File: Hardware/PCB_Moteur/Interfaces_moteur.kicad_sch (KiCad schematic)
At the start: 47 parts, among them J3 Conn_01x02, J6 Conn_01x06_Pin, U12 MCP1802T-5002I/OT, U2 ISOW1044, U4 LSF0204PWR

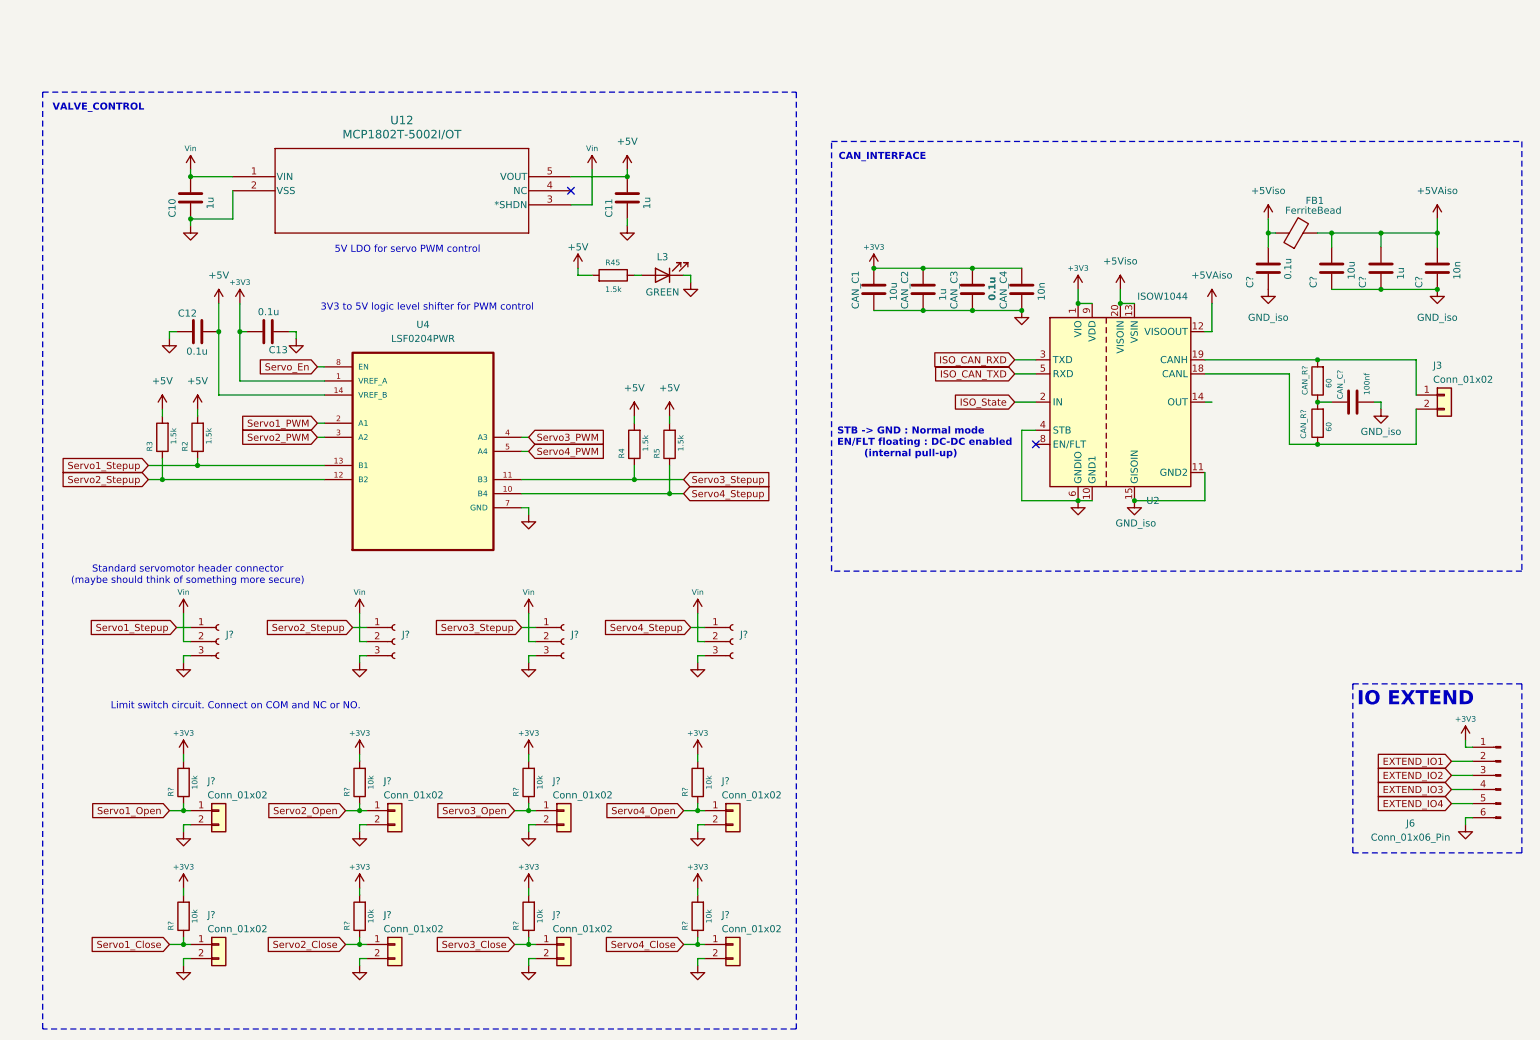
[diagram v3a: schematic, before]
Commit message: fix: LDO 5V SHDN + REFs (missing) + change EN valves controller connection + fix intrumental ampliop + add pull-down to sleep pins
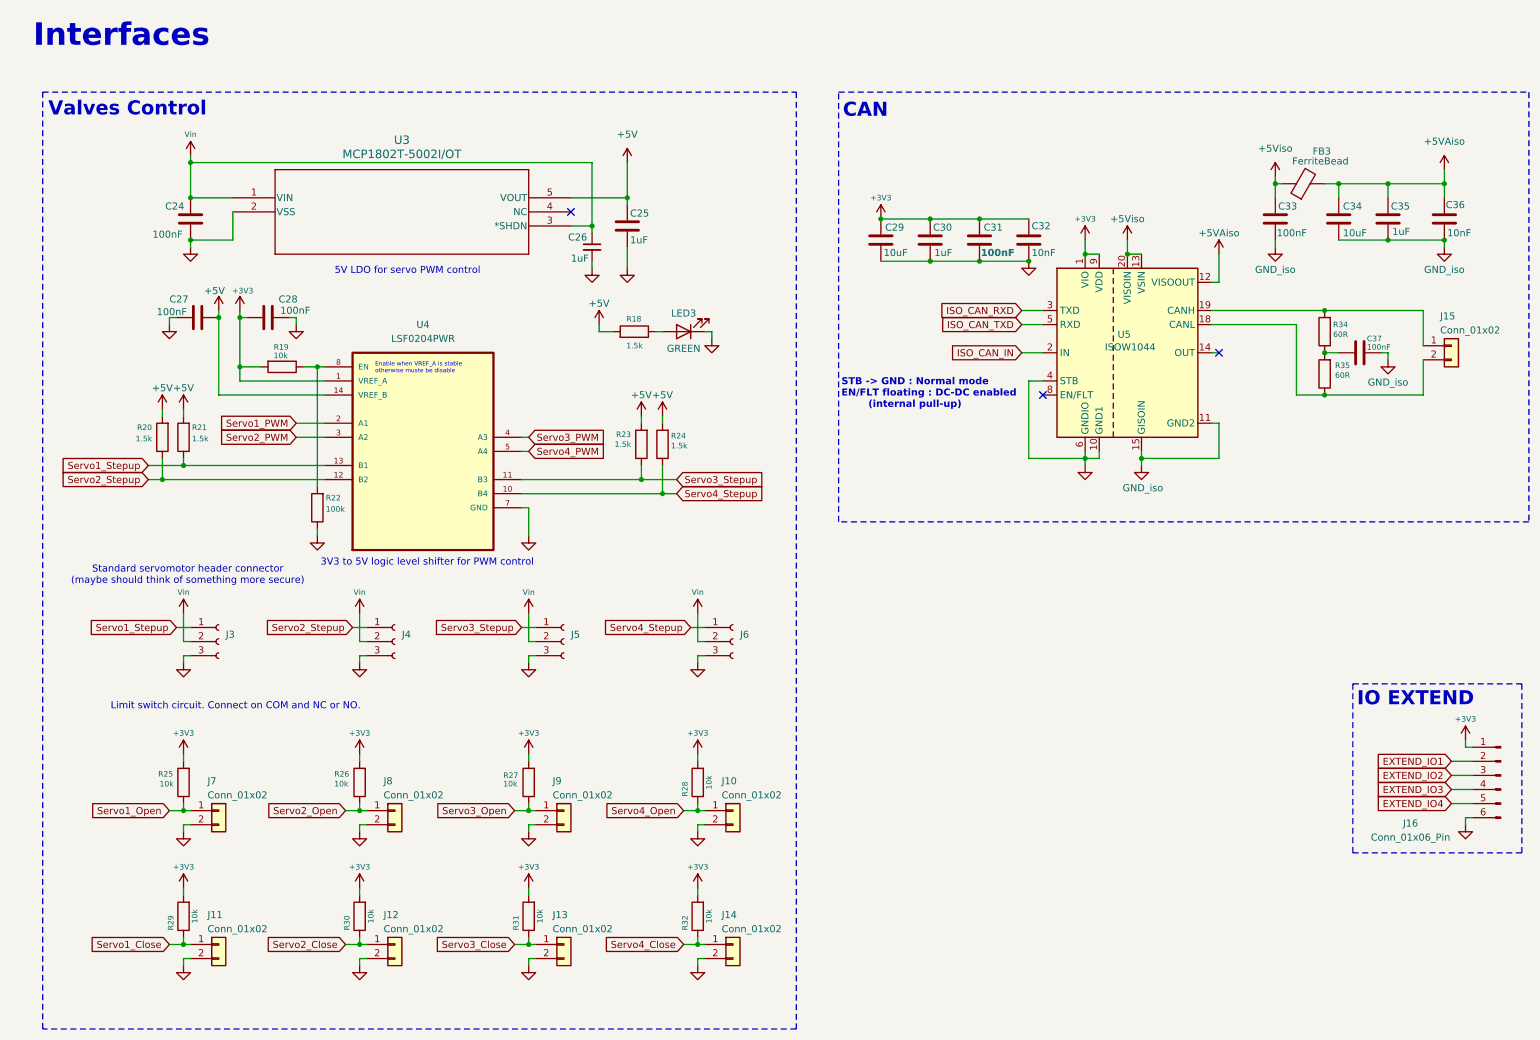
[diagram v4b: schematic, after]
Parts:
- added C26: 1uF, Capacitor_SMD:C_0603_1608Metric, symbol Device:C_Small
- added R19: 10k, Resistor_SMD:R_0805_2012Metric, symbol Device:R
- added R22: 100k, Resistor_SMD:R_0805_2012Metric, symbol Device:R
- C24: renamed from C10; value 1u -> 100nF
- C25: renamed from C11; value 1u -> 1uF
- C27: renamed from C12; value 0.1u -> 100nF
- C28: renamed from C13; value 0.1u -> 100nF
- C29: renamed from CAN_C1; value 10u -> 10uF
- C30: renamed from CAN_C2; value 1u -> 1uF
- C31: renamed from CAN_C3; value 0.1u -> 100nF
- C32: renamed from CAN_C4; value 10n -> 10nF
- C33: renamed from C?; value 0.1u -> 100nF
- C34: renamed from C?; value 10u -> 10uF
- C35: renamed from C?; value 1u -> 1uF
- C36: renamed from C?; value 10n -> 10nF
- C37: renamed from CAN_C?; value 100nf -> 100nF
- R34, R35: renamed from CAN_R?; value 60 -> 60R
- gave numbers to parts that had none: 20
- renumbered FB1 to FB3, J3 to J15, J6 to J16, L3 to LED3, R45 to R18, R3 to R20, R2 to R21, R4 to R23, R5 to R24, U12 to U3, U2 to U5
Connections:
- net +3V3: now also R19.2
- net GND: now also C26.2, R22.1
- net Vin: now also C26.1
- net ISO_State renamed ISO_CAN_IN
- net Servo_En: no longer names the net of U4.8 (EN)
- net Servo_En: now also R19.1, R22.2
- no-connect marks 2 -> 3
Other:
- note added: "CAN"
- note added: "Enable when VREF_A is stable otherwise muste be disable"
- note added: "Interfaces"
- note added: "Valves Control"
- note removed: "CAN_INTERFACE"
- note removed: "VALVE_CONTROL"
- moved on the sheet: C24, C25, C27, C28, C29, C30, C31, C32, C33, C34, C35, C36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

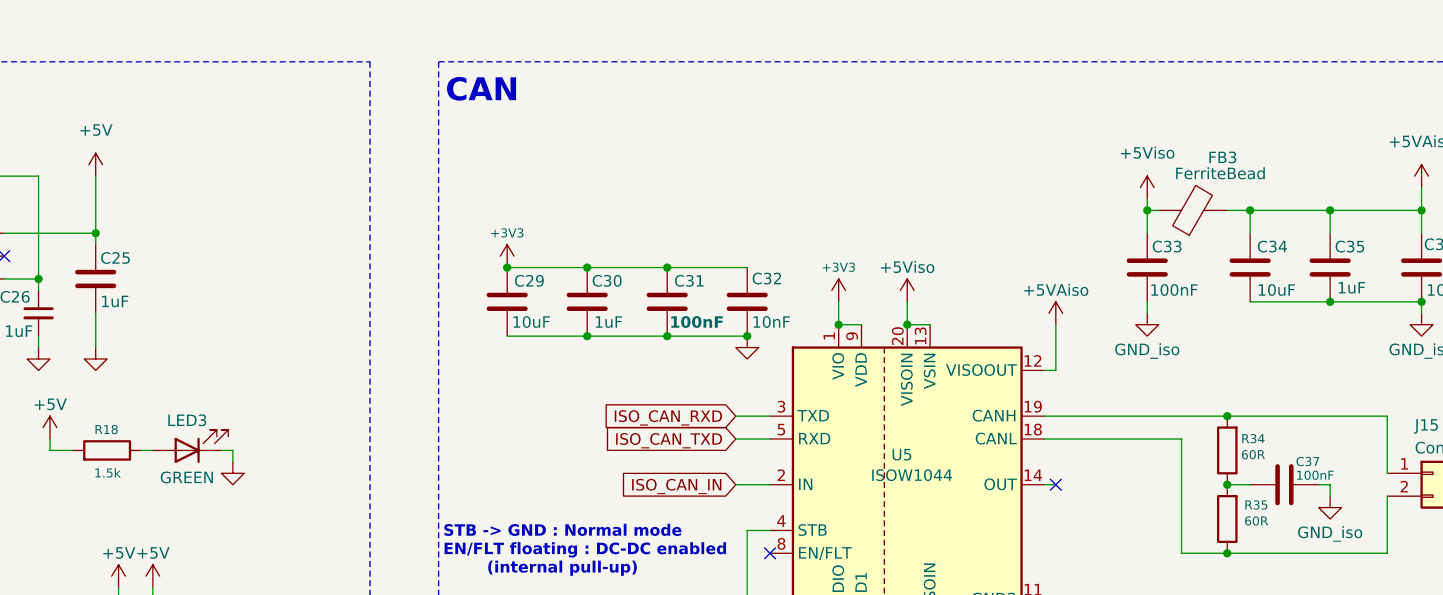
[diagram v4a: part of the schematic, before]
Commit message: wip : minor corrections and fix footprints except connectors
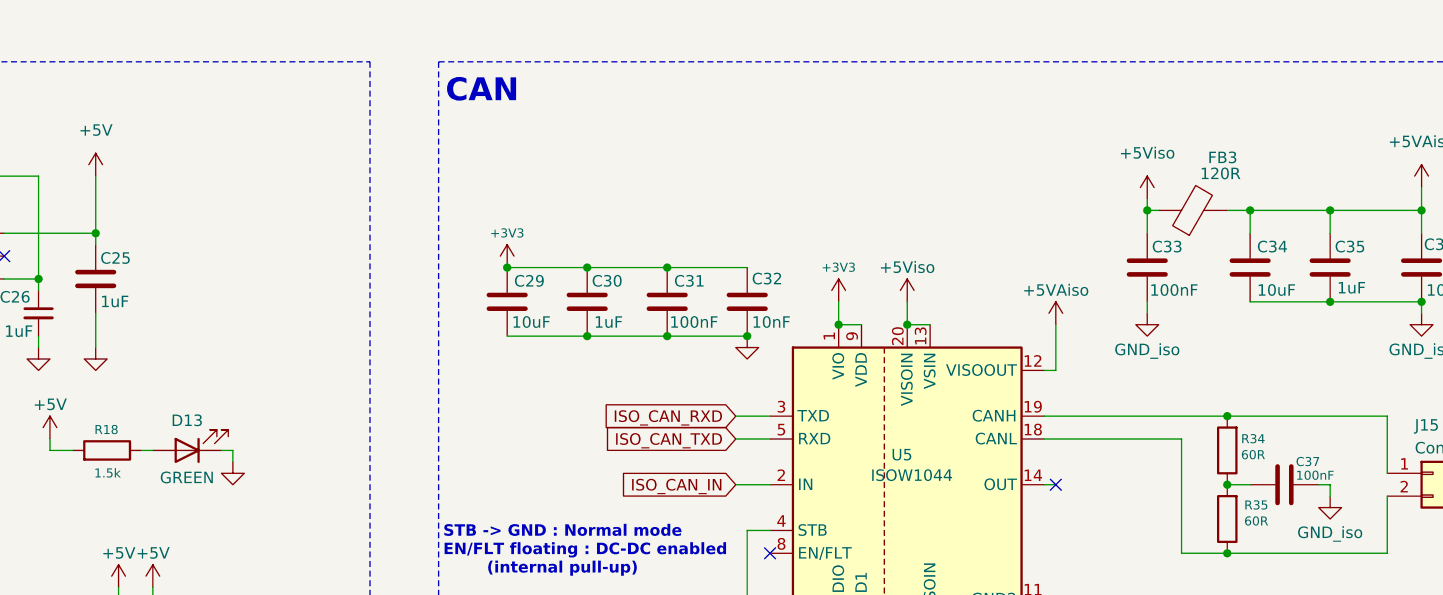
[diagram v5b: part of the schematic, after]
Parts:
- removed LED3: GREEN, LED_SMD:LED_0603_1608Metric, symbol Device:LED
- added D13: GREEN, ODB:LED_QBLP601-AG15, symbol Device:LED
- C24, C25, C27, C28, C29, C30, C31, C32, C33, C34, C35, C36: footprint (none) -> Capacitor_SMD:C_0805_2012Metric
- C26: footprint Capacitor_SMD:C_0603_1608Metric -> Capacitor_SMD:C_0805_2012Metric
- FB3: value FerriteBead -> 120R; footprint (none) -> Inductor_SMD:L_0805_2012Metric
- U3: footprint SOT-23-5_MC_MCH -> Package_TO_SOT_SMD:SOT-23-5
- U4: footprint LSF0204PWR:SOP65P640X120-14N -> Package_SO:TSSOP-14_4.4x5mm_P0.65mm
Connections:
- net GND: now also D13.1 (K)
- net at R18.1: now also D13.2 (A)
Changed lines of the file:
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@@
 			)
 		)
-		(property "Footprint" "Capacitor_SMD:C_0603_1608Metric"
+		(property "Footprint" "Capacitor_SMD:C_0805_2012Metric"
 			(at 114.3 54.61 0)
 			(effects
@@
 	)
 	(symbol
-		(lib_id "Device:LED")
-		(at 130.81 69.85 180)
-		(unit 1)
-		(exclude_from_sim no)
-		(in_bom yes)
-		(on_board yes)
-		(dnp no)
-		(property "Reference" "LED3"
-			(at 130.81 66.548 0)
-			(effects
-				(font
-					(size 1.27 1.27)
-				)
-			)
-		)
-		(property "Value" "GREEN"
-			(at 130.81 72.898 0)
-			(effects
-				(font
-					(size 1.27 1.27)
-				)
-			)
-		)
-		(property "Footprint" "LED_SMD:LED_0603_1608Metric"
-			(at 130.81 69.85 0)
-			(effects
-				(font
-					(size 1.27 1.27)
-				)
-				(hide yes)
-			)
-		)
-		(property "Datasheet" "~"
-			(at 130.81 69.85 0)
-			(effects
-				(font
-					(size 1.27 1.27)
-				)
-				(hide yes)
-			)
-		)
-		(property "Description" "Light emitting diode"
-			(at 130.81 69.85 0)
-			(effects
-				(font
-					(size 1.27 1.27)
-				)
-				(hide yes)
-			)
-		)
-		(pin "1"
-		)
-		(pin "2"
-		)
-		(instances
-			(project "PCB_moteur"
-				(path "/b0d87684-7b1c-41d8-8358-755aa327573e/a8ed0c04-b51e-4eec-84d1-0b2303d57d27"
-					(reference "LED3")
-					(unit 1)
-				)
-			)
-		)
-	)
-	(symbol
 		(lib_id "power:GND")
 		(at 133.35 129.54 0)
@@
 			)
 		)
-		(property "Footprint" ""
+		(property "Footprint" "Capacitor_SMD:C_0805_2012Metric"
 			(at 268.9352 53.34 0)
 			(effects
@@
 			)
 		)
-		(property "Footprint" "LSF0204PWR:SOP65P640X120-14N"
+		(property "Footprint" "Package_SO:TSSOP-14_4.4x5mm_P0.65mm"
 			(at 83.82 91.44 0)
 			(effects
@@
 			)
 		)
-		(property "Footprint" ""
+		(property "Footprint" "Capacitor_SMD:C_0805_2012Metric"
 			(at 194.0052 57.15 0)
 			(effects
@@
 	)
 	(symbol
+		(lib_id "Device:LED")
+		(at 130.81 69.85 180)
+		(unit 1)
+		(exclude_from_sim no)
+		(in_bom yes)
+		(on_board yes)
+		(dnp no)
+		(property "Reference" "D13"
+			(at 130.81 66.548 0)
+			(effects
+				(font
+					(size 1.27 1.27)
+				)
+			)
+		)
+		(property "Value" "GREEN"
+			(at 130.81 72.898 0)
+			(effects
+				(font
+					(size 1.27 1.27)
+				)
+			)
+		)
+		(property "Footprint" "ODB:LED_QBLP601-AG15"
+			(at 130.81 69.85 0)
+			(effects
+				(font
+					(size 1.27 1.27)
+				)
+				(hide yes)
+			)
+		)
+		(property "Datasheet" "https://www.digikey.ca/en/products/detail/qt-brightek-qtb/QBLP601-AG15/16499667"
+			(at 130.81 69.85 0)
+			(effects
+				(font
+					(size 1.27 1.27)
+				)
+				(hide yes)
+			)
+		)
+		(property "Description" "Light emitting diode"
+			(at 130.81 69.85 0)
+			(effects
+				(font
+					(size 1.27 1.27)
+				)
+				(hide yes)
+			)
+		)
+		(property "DigiKey_Part_Number" "1516-QBLP601-AG15CT-ND"
+			(at 130.81 69.85 0)
+			(effects
+				(font
+					(size 1.27 1.27)
+				)
+				(hide yes)
+			)
+		)
+		(property "Purchase-URL" ""
+			(at 130.81 69.85 0)
+			(effects
+				(font
+					(size 1.27 1.27)
+				)
+				(hide yes)
+			)
+		)
+		(property "Sim.Device" ""
+			(at 130.81 69.85 0)
+			(effects
+				(font
+					(size 1.27 1.27)
+				)
+				(hide yes)
+			)
+		)
+		(property "Sim.Pins" ""
+			(at 130.81 69.85 0)
+			(effects
+				(font
+					(size 1.27 1.27)
+				)
+				(hide yes)
+			)
+		)
+		(property "Sim.Type" ""
+			(at 130.81 69.85 0)
+			(effects
+				(font
+					(size 1.27 1.27)
+				)
+				(hide yes)
+			)
+		)
+		(property "Manufacturer_Part_Number" "QBLP601-AG15"
+			(at 130.81 69.85 0)
+			(effects
+				(font
+					(size 1.27 1.27)
+				)
+				(hide yes)
+			)
+		)
+		(pin "1"
+		)
+		(pin "2"
+		)
+		(instances
+			(project "PCB_moteur"
+				(path "/b0d87684-7b1c-41d8-8358-755aa327573e/a8ed0c04-b51e-4eec-84d1-0b2303d57d27"
+					(reference "D13")
+					(unit 1)
+				)
+			)
+		)
+	)
+	(symbol
 		(lib_id "Device:R")
 		(at 127 90.17 180)
@@
 			)
 		)
-		(property "Value" "FerriteBead"
+		(property "Value" "120R"
 			(at 245.618 39.116 90)
 			(effects
@@
 			)
 		)
-		(property "Footprint" ""
+		(property "Footprint" "Inductor_SMD:L_0805_2012Metric"
 			(at 242.57 44.958 90)
 			(effects
@@
 			)
 		)
-		(property "Footprint" ""
+		(property "Footprint" "Capacitor_SMD:C_0805_2012Metric"
 			(at 42.8752 53.34 0)
 			(effects
@@
 			)
 		)
-		(property "Footprint" ""
+		(property "Footprint" "Capacitor_SMD:C_0805_2012Metric"
 			(at 121.6152 54.61 0)
 			(effects
@@
 			)
 		)
-		(property "Footprint" ""
+		(property "Footprint" "Capacitor_SMD:C_0805_2012Metric"
 			(at 249.8852 53.34 0)
 			(effects
@@
 			)
 		)
-		(property "Footprint" ""
+		(property "Footprint" "Capacitor_SMD:C_0805_2012Metric"
 			(at 258.7752 53.34 0)
 			(effects
@@
 			)
 		)
-		(property "Footprint" ""
+		(property "Footprint" "Capacitor_SMD:C_0805_2012Metric"
 			(at 238.4552 53.34 0)
 			(effects
@@
 			)
 		)
-		(property "Footprint" "SOT-23-5_MC_MCH"
+		(property "Footprint" "Package_TO_SOT_SMD:SOT-23-5"
 			(at 49.53 45.72 0)
 			(effects
@@
 			)
 		)
-		(property "Footprint" ""
+		(property "Footprint" "Capacitor_SMD:C_0805_2012Metric"
 			(at 167.3352 57.15 0)
 			(effects
@@
 			)
 		)
-		(property "Footprint" ""
+		(property "Footprint" "Capacitor_SMD:C_0805_2012Metric"
 			(at 39.37 68.2752 0)
 			(effects
@@
 			)
 		)
-		(property "Footprint" ""
+		(property "Footprint" "Capacitor_SMD:C_0805_2012Metric"
 			(at 176.2252 57.15 0)
 			(effects
@@
 				(font
 					(size 1.27 1.27)
-					(thickness 0.254)
-					(bold yes)
+					(thickness 0.1588)
 				)
 				(justify left)
 			)
 		)
-		(property "Footprint" ""
+		(property "Footprint" "Capacitor_SMD:C_0805_2012Metric"
 			(at 185.1152 57.15 0)
 			(effects
@@
 			)
 		)
-		(property "Footprint" ""
+		(property "Footprint" "Capacitor_SMD:C_0805_2012Metric"
 			(at 59.69 66.3448 0)
 			(effects
